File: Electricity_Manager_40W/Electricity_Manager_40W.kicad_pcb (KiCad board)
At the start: 2 copper layers, 100 x 77 mm, 195 parts, among them IC2 MAIN_SHUTDOWN, IC3 RELAY_STATE, IC4 ADC_RST, J1 SERIAL, P1 SWD, P10 EMERGENCY, P11 EMERGENCY, P12 FRAME_GRAND, P13 BATT_IN, P15 OUT_B, P16 BATT_IN, P17 OUT_A, P2 CAN, P3 CAN, P4 EMERGENCY_SIGNAL, P5 EMERGENCY_SIGNAL, P6 12V_OUT, P7 12V_OUT, P9 MAIN_SW, Q1 FET_N, Q2 NPN, Q3 NPN, Q4 FET_N, Q7 FET_N, SW1 RST, SW2 SW0, SW3 SW1, U1 MAX3051, U10 BD9G101G, U11 OUTA_CHECK, U12 V23134J1052D642, U13 ACS70331, U14 OUTB_CHECK, U15 BD33FA1, U16 LOGO, U17 LOGO, U18 LOGO, U19 MCP2221A, U2 STM32F405RG, U20 OSRB38C9AA, U21 OSRB38C9AA, U22 HSIN_946, U23 LOGO, U24 LOGO, U25 LOGO, U3 FULL COLOR, U4 AQM0802_BL, U5 AP3211, U6 SI8900, U7 AZ1086H, U8 V23134J1052D642, U9 RPA60-12FW/N, X1 8MHz

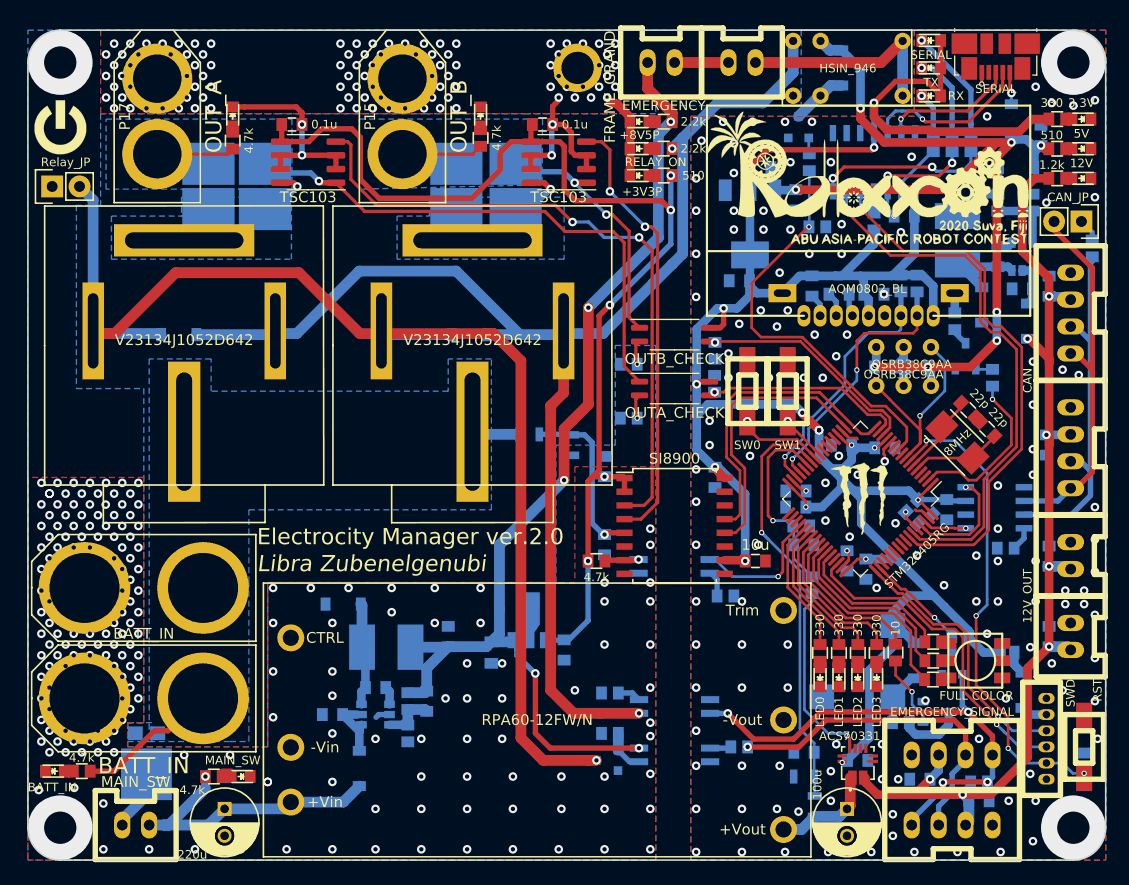
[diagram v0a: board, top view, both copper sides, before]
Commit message: electrocity -> electricity
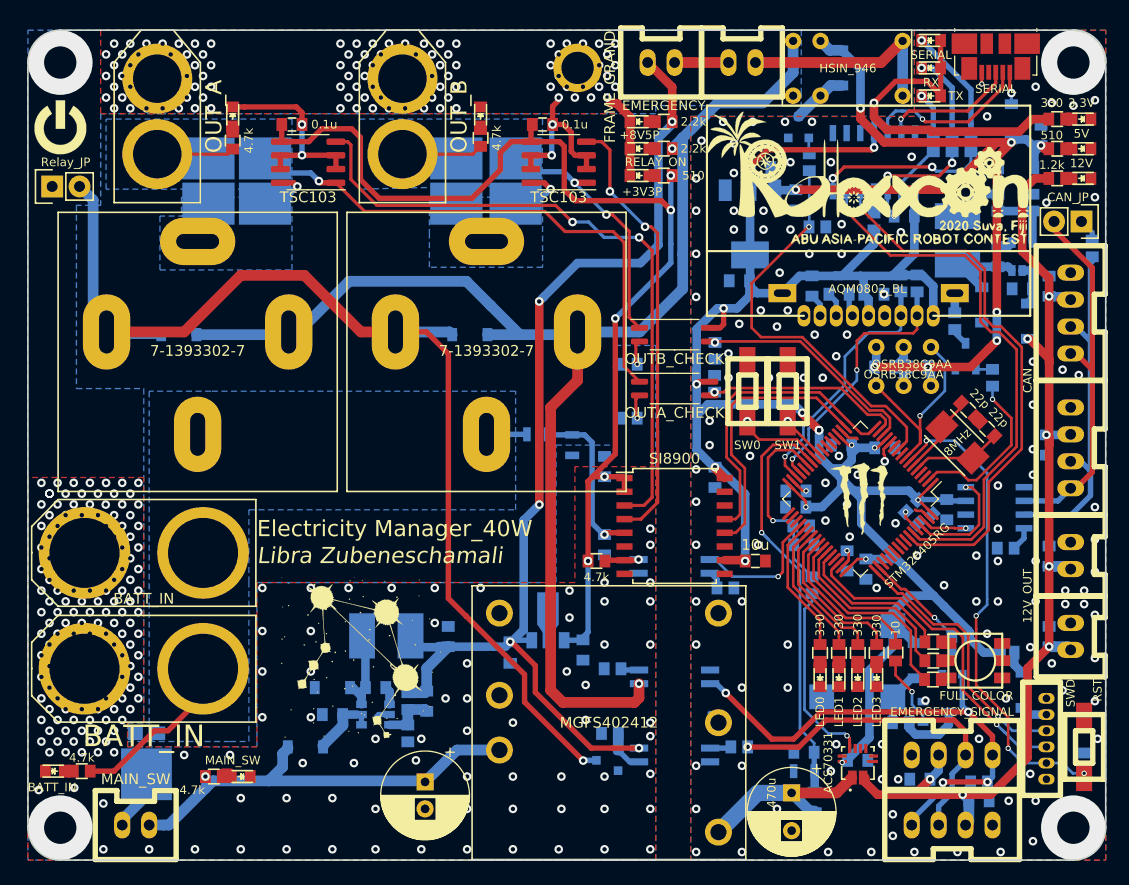
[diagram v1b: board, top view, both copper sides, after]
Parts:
- removed U24: LOGO, Mizz_lib:Dodaitos_15x15_silk
- added DCDC1: MGFS402412, Mizz_lib:MGFS402412, F.Cu at (91.8, 162.2)
- added RL1: 7-1393302-7, Mizz_lib:7-1393302-7, F.Cu at (63.8, 126.0)
- added RL2: 7-1393302-7, Mizz_lib:7-1393302-7, F.Cu at (90.5, 126.0)
- C32: footprint Capacitors_ThroughHole:C_Radial_D6.3_L11.2_P2.5 -> Capacitor_THT:CP_Radial_D8.0mm_P2.50mm
- C35: value 100u -> 470u; footprint Capacitors_ThroughHole:C_Radial_D6.3_L11.2_P2.5 -> Capacitor_THT:CP_Radial_D8.0mm_P3.50mm
- D26: value RX -> TX
- D27: value TX -> RX
- R52: value 49.9k -> 10k
- R53: value 10k -> 1k
- U12: value V23134J1052D642 -> LOGO; footprint Mizz_lib:V23134J1052D642 -> Mizz_lib:Libra_15x15_silk
- U13: value ACS70331 -> LOGO; footprint Mizz_lib:ALLEGRO_ACS70331EESATR-005U3 -> Mizz_lib:RP_KIT_Logo_mask_15.0x15.0
- U8: value V23134J1052D642 -> ACS70331; footprint Mizz_lib:V23134J1052D642 -> Mizz_lib:ALLEGRO_ACS70331EESATR-005U3
- U9: value RPA60-12FW/N -> LOGO; footprint Mizz_lib:RPA60-24xxSFW -> Mizz_lib:Mega_Fusigibana_15x9_silk; moved to B.Cu
- moved U8 73.5 mm to (125.0, 166.0), turned to 90 degrees
- moved U13 50.6 mm to (74.5, 169.2), turned to 0 degrees
- moved U12 30.8 mm to (79.0, 156.2)
- moved C32 18.8 mm to (84.8, 167.8)
- moved U9 18.4 mm to (78.0, 168.5), turned to 180 degrees
- moved U25 15.3 mm to (67.8, 169.8)
- moved D24 7.81 mm to (76.2, 159.0)
- moved D21 5.39 mm to (73.8, 164.5), turned to 0 degrees
- moved C35 5.35 mm to (118.9, 168.8)
- moved P16 3.25 mm to (58.8, 146.5)
- moved IC3 2.75 mm to (108.0, 158.0)
- moved P13 2.75 mm to (58.8, 157.2)
- moved R11 2.26 mm to (102.2, 157.2)
- moved C37 1.75 mm to (92.8, 155.8)
- moved C43 1.75 mm to (99.5, 155.5)
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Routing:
- net /24V: track 27.4 -> 40.4 mm
- net Net-(C35-Pad1): track 9.71 -> 17.3 mm
- net /Relay_Out: track 115.4 -> 109.0 mm
- net /Coil: track 126.6 -> 129.5 mm
- net +8V: track 98.0 -> 100.6 mm
- net 3V3: track 107.3 -> 105.7 mm
- net Net-(C36-Pad2): track 9.63 -> 8.48 mm
- net /Relay_state: track 46.6 -> 47.8 mm
- net Net-(IC4-Pad2): track 2.46 -> 1.71 mm
- net +BATT: track 17.7 -> 17.1 mm
- net GNDPWR: vias 288 -> 297
- net GND: vias 135 -> 129
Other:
- board text added: "Designed by A.Mizuta in 2019/11/18."
- board text added: "Electricity Manager_40W"
- board text added: "Libra Zubeneschamali"
- board text added: "Pocket Monster "Mega Fushigibana""
- board text removed: "Designed by A.Mizuta in 2019/11/05."
- board text removed: "Electrocity Manager ver.2.0"
- board text removed: "Libra Zubenelgenubi"
- board text removed: "Pocket Monster "Dodaitos""
